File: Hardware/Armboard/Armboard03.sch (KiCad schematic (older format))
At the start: 8 parts

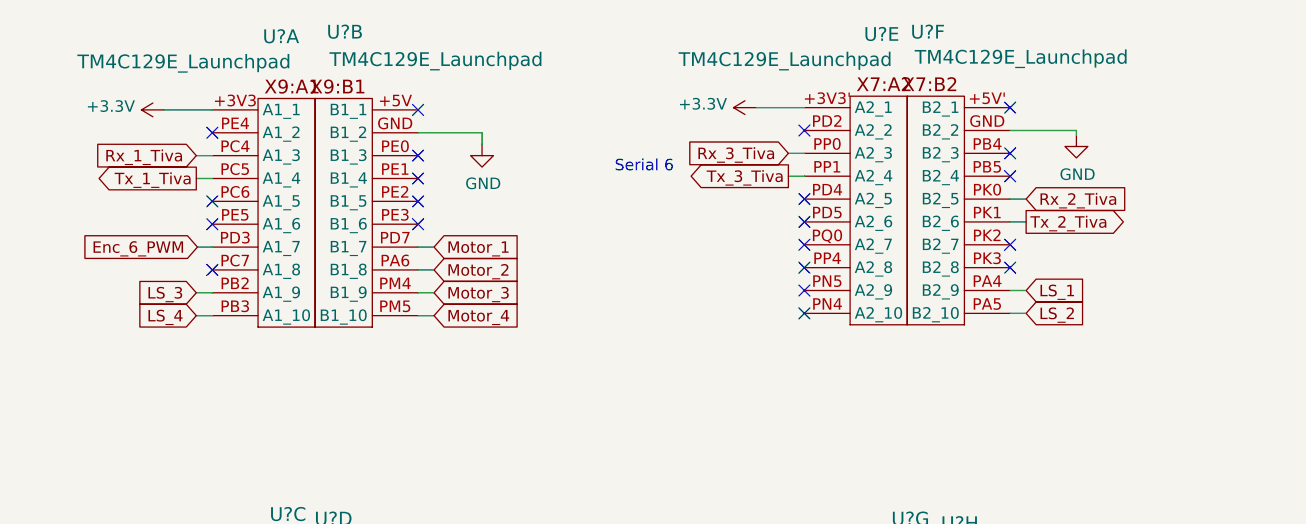
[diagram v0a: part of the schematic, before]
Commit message: Added Software LEDs
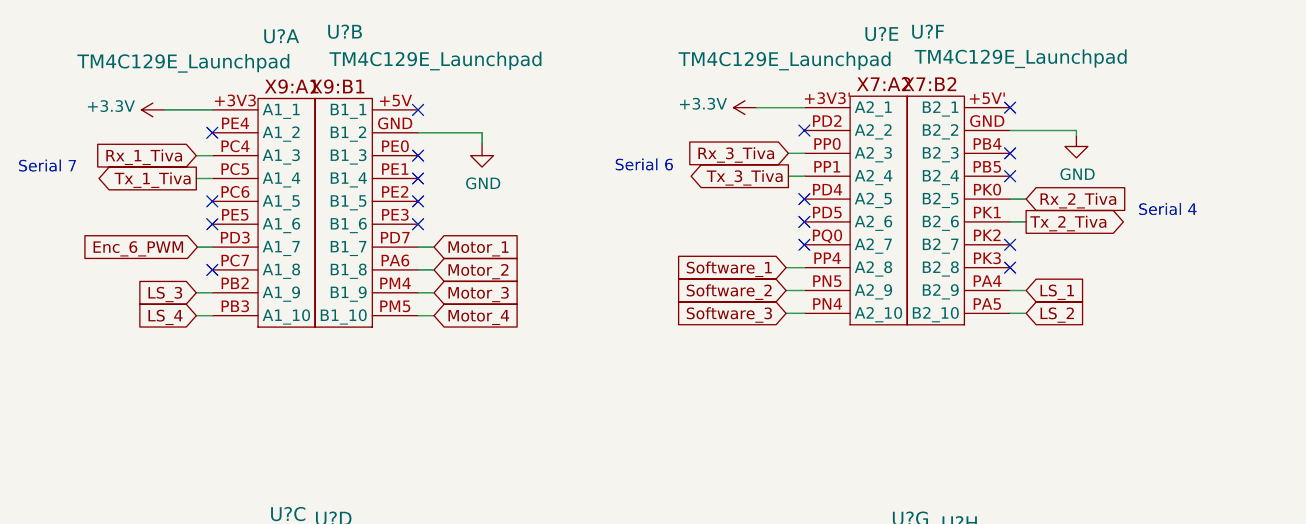
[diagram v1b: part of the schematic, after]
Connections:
- net Software_3: now reaches U?.PN4 (A2_10)
- net Software_2: now reaches U?.PN5 (A2_9)
- net Software_1: now reaches U?.PP4 (A2_8)
- no-connect marks 46 -> 43
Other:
- note added: "Serial 4"
- note added: "Serial 7"
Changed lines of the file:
@@
 NoConn ~ 6200 2940
 NoConn ~ 6200 3040
-NoConn ~ 6200 3140
-NoConn ~ 6200 3240
-NoConn ~ 6200 3340
 NoConn ~ 7100 2440
 NoConn ~ 7100 2640
@@
 	3610 3050 3545 3050
 NoConn ~ 6320 4670
+Text Notes 2760 2735 0    50   ~ 0
+Serial 7
+Text Notes 7660 2925 0    50   ~ 0
+Serial 4
+Text GLabel 6120 3140 0    50   Input ~ 0
+Software_1
+Wire Wire Line
+	6120 3140 6200 3140
+Text GLabel 6120 3240 0    50   Input ~ 0
+Software_2
+Wire Wire Line
+	6120 3240 6200 3240
+Text GLabel 6120 3340 0    50   Input ~ 0
+Software_3
+Wire Wire Line
+	6120 3340 6200 3340
 $EndSCHEMATC
